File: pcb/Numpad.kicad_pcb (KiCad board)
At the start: 2 copper layers, 76.2 x 114.3 mm, 61 parts, among them P1 USB-MICRO-B, P2 HOLE, P3 HOLE, P4 HOLE, P5 HOLE, SW1 F1, SW10 8, SW11 9, SW12 PLUS, SW13 4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

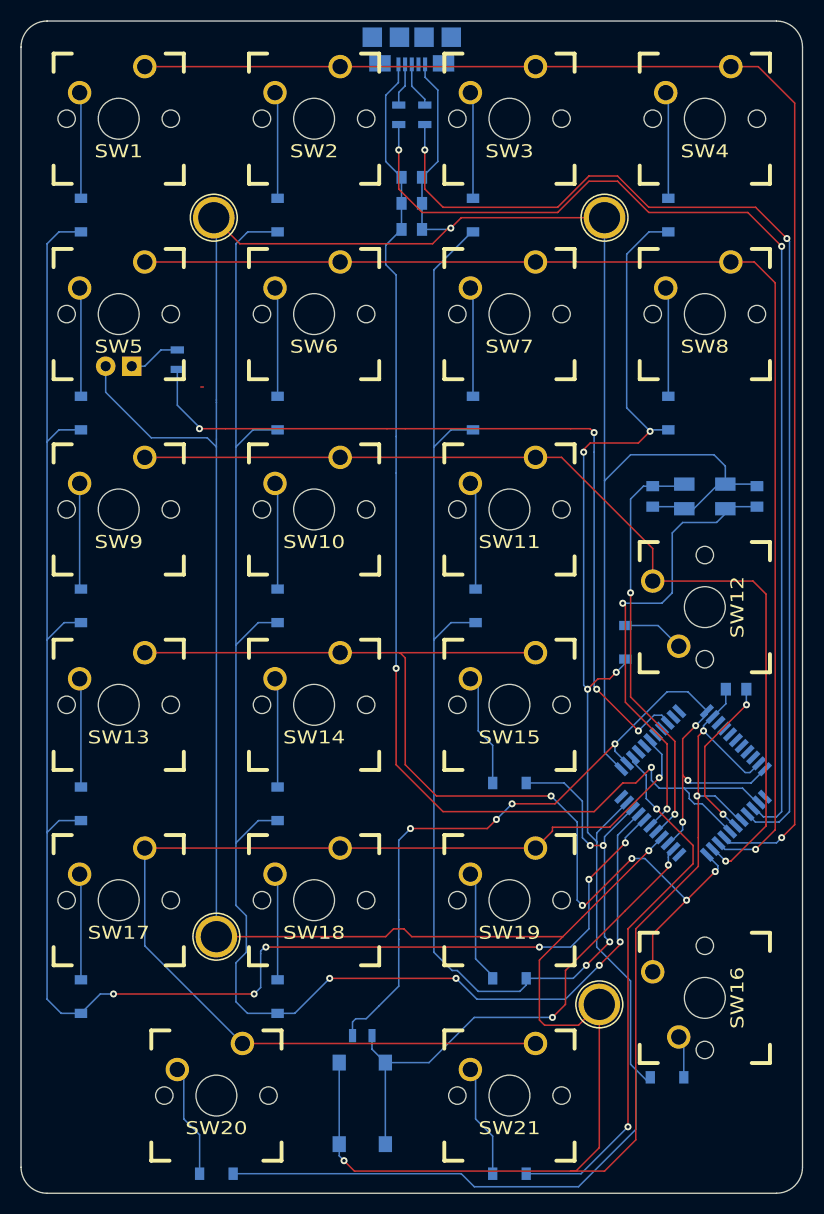
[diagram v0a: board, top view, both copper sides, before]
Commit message: Add my own key footprints
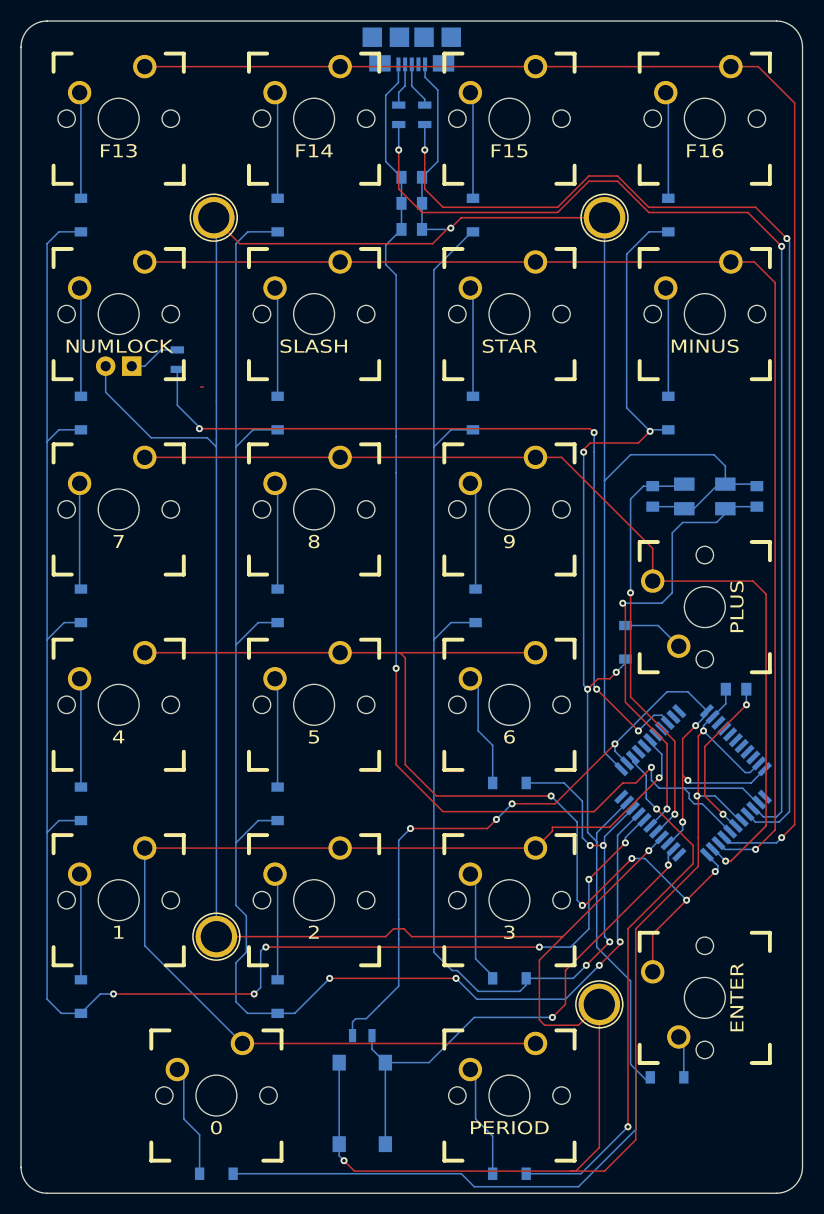
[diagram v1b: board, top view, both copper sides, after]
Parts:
- SW1: value F1 -> F13; footprint Keyboard:CHERRY_PLATE_100H -> Tim's Cherry MX:CHERRY_PLATE_100H
- SW10, SW11, SW13, SW14, SW15, SW17, SW18, SW19, SW21, SW5, SW6, SW7, SW8, SW9: footprint Keyboard:CHERRY_PLATE_100H -> Tim's Cherry MX:CHERRY_PLATE_100H
- SW12, SW16: footprint Keyboard:CHERRY_PLATE_200V -> Tim's Cherry MX:CHERRY_PLATE_200V
- SW2: value F2 -> F14; footprint Keyboard:CHERRY_PLATE_100H -> Tim's Cherry MX:CHERRY_PLATE_100H
- SW20: footprint Keyboard:CHERRY_PLATE_200H -> Tim's Cherry MX:CHERRY_PLATE_200H
- SW3: value F3 -> F15; footprint Keyboard:CHERRY_PLATE_100H -> Tim's Cherry MX:CHERRY_PLATE_100H
- SW4: value F4 -> F16; footprint Keyboard:CHERRY_PLATE_100H -> Tim's Cherry MX:CHERRY_PLATE_100H

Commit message: move drill hole
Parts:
- moved P4 13.1 mm to (85.1, 130.8)
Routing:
- net /COL1: track 150.0 -> 148.8 mm
- net GND: track 409.2 -> 409.4 mm, vias 5 -> 6
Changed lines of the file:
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@@
     (links 106)
     (no_connects 0)
-    (area 65.989999 54.559999 142.290001 168.960001)
+    (area 65.938399 53.209199 142.341601 170.1324)
     (thickness 1.6)
     (drawings 8)
-    (tracks 561)
+    (tracks 565)
     (zones 0)
     (modules 61)
@@
     (visible_elements 7FFFFFFF)
     (pcbplotparams
-      (layerselection 0x00030_80000001)
+      (layerselection 0x01000_00000000)
       (usegerberextensions false)
       (excludeedgelayer true)
@@
       (outputformat 1)
       (mirror false)
-      (drillshape 1)
+      (drillshape 0)
       (scaleselection 1)
-      (outputdirectory ""))
+      (outputdirectory ../../../../../Desktop/))
   )
   (net 0 "")
@@
   )
   (module Connect:1pin (layer F.Cu)
-    (at 85.09 143.891)
+    (at 85.09 130.81)
     (descr "module 1 pin (ou trou mecanique de percage)")
     (tags DEV)
@@
   (gr_arc (start 68.58 166.37) (end 68.58 168.91) (angle 90) (layer Edge.Cuts) (width 0.1))
   (gr_arc (start 68.58 57.15) (end 66.04 57.15) (angle 90) (layer Edge.Cuts) (width 0.1))
-  (segment (start 83.566 90.297) (end 83.82 90.297) (width 0.1524) (layer F.Cu) (net 0))
   (segment (start 136.763 119.761) (end 136.763 121.269) (width 0.1524) (layer B.Cu) (net 1))
   (segment (start 134.493 131.953) (end 135.61693 133.07693) (width 0.1524) (layer B.Cu) (net 1))
@@
   (segment (start 136.763 121.269) (end 136.779 121.285) (width 0.1524) (layer B.Cu) (net 1))
   (segment (start 135.61693 133.07693) (end 135.74393 133.07693) (width 0.1524) (layer B.Cu) (net 1))
+  (segment (start 85.09 130.81) (end 85.09 96.012) (width 0.1524) (layer B.Cu) (net 2))
+  (segment (start 85.09 130.81) (end 85.09 144.018) (width 0.1524) (layer B.Cu) (net 2))
+  (via (at 85.09 144.018) (size 0.6858) (drill 0.3302) (layers F.Cu B.Cu) (net 2))
   (segment (start 74.295 88.265) (end 74.295 90.805) (width 0.1524) (layer B.Cu) (net 2))
+  (segment (start 85.09 96.012) (end 85.09 96.139) (width 0.1524) (layer B.Cu) (net 2))
+  (segment (start 74.295 90.805) (end 78.74 95.25) (width 0.1524) (layer B.Cu) (net 2))
+  (segment (start 78.74 95.25) (end 84.201 95.25) (width 0.1524) (layer B.Cu) (net 2))
   (segment (start 84.201 95.25) (end 85.09 96.139) (width 0.1524) (layer B.Cu) (net 2))
-  (segment (start 78.74 95.25) (end 84.201 95.25) (width 0.1524) (layer B.Cu) (net 2))
-  (segment (start 74.295 90.805) (end 78.74 95.25) (width 0.1524) (layer B.Cu) (net 2))
   (segment (start 85.09 74.041) (end 85.09 91.567) (width 0.1524) (layer B.Cu) (net 2))
+  (segment (start 85.09 91.821) (end 85.09 95.377) (width 0.1524) (layer B.Cu) (net 2))
+  (segment (start 85.09 95.377) (end 85.09 96.012) (width 0.1524) (layer B.Cu) (net 2))
   (segment (start 85.09 91.567) (end 85.09 91.821) (width 0.1524) (layer B.Cu) (net 2))
-  (segment (start 85.09 95.377) (end 85.09 96.139) (width 0.1524) (layer B.Cu) (net 2))
-  (segment (start 85.09 96.139) (end 85.09 143.891) (width 0.1524) (layer B.Cu) (net 2))
-  (segment (start 85.09 91.821) (end 85.09 95.377) (width 0.1524) (layer B.Cu) (net 2))
   (segment (start 85.09 74.041) (end 84.836 73.787) (width 0.1524) (layer B.Cu) (net 2))
   (segment (start 132.08 130.175) (end 131.953 130.175) (width 0.1524) (layer F.Cu) (net 2))
@@
   (segment (start 71.882 61.722) (end 71.755 61.595) (width 0.1524) (layer B.Cu) (net 7))
   (segment (start 71.755 71.771) (end 71.882 71.898) (width 0.1524) (layer B.Cu) (net 7))
+  (segment (start 89.17 132.572) (end 89.17 130.191) (width 0.1524) (layer B.Cu) (net 8))
+  (segment (start 86.995 128.016) (end 86.995 115.443) (width 0.1524) (layer B.Cu) (net 8))
+  (segment (start 89.17 130.191) (end 86.995 128.016) (width 0.1524) (layer B.Cu) (net 8))
   (segment (start 91.059 94.472) (end 88.662 94.472) (width 0.1524) (layer B.Cu) (net 8))
   (segment (start 88.662 94.472) (end 86.995 96.139) (width 0.1524) (layer B.Cu) (net 8))
@@
   (segment (start 88.011 141.859) (end 86.995 140.843) (width 0.1524) (layer B.Cu) (net 8))
   (segment (start 86.995 140.843) (end 86.995 134.747) (width 0.1524) (layer B.Cu) (net 8))
-  (segment (start 86.995 134.747) (end 86.995 115.443) (width 0.1524) (layer B.Cu) (net 8))
   (segment (start 86.995 115.443) (end 86.995 96.139) (width 0.1524) (layer B.Cu) (net 8))
   (segment (start 86.995 96.139) (end 86.995 76.327) (width 0.1524) (layer B.Cu) (net 8))
